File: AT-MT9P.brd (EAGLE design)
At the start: 38 x 34 mm, 3 parts

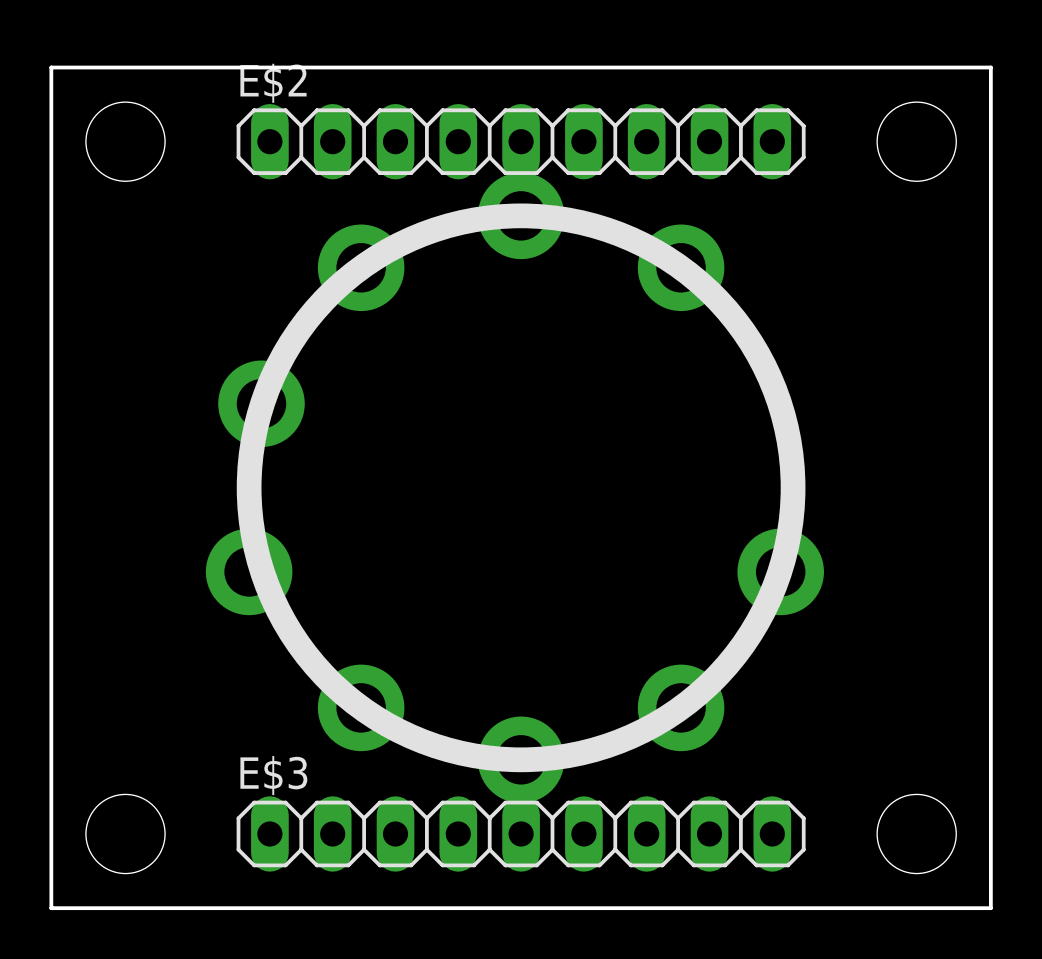
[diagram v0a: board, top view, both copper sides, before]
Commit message: [fix]ピンヘッダが逆だった
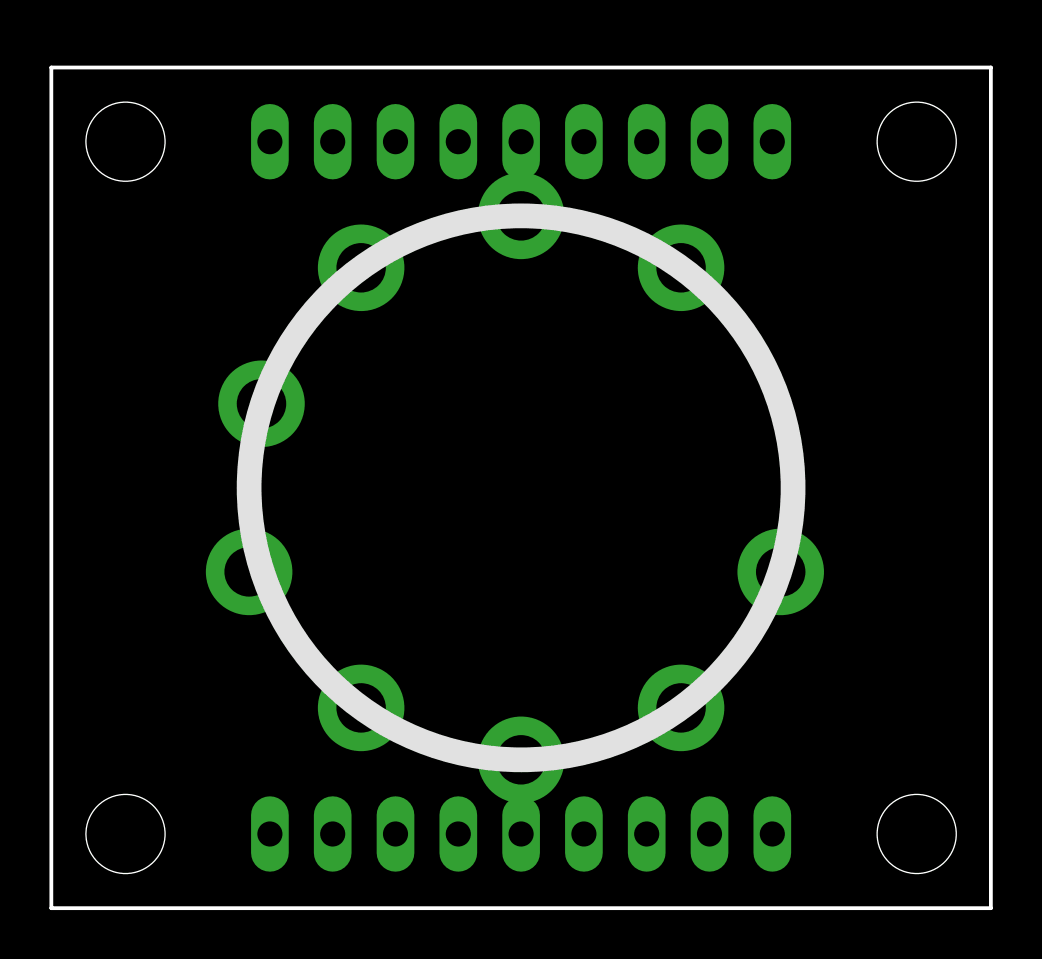
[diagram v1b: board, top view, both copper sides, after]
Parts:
- flipped E$2 to the bottom
- flipped E$3 to the bottom
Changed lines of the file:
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@@
 </layers>
 <board>
-<fusionsync huburn="a.cGVyc29uYWw6dWUyZDlmMDVj" projecturn="a.cGVyc29uYWw6dWUyZDlmMDVjIzIwMTgxMjMwMTY3NjU5OTU2" f3durn="urn:adsk.wipprod:dm.lineage:NYwnF4SlTam06u2sAxt6oQ" pcbguid="4a25c511-59d3-438b-b27a-b959e0cbe7cb" lastpulledtime="" lastsyncedchangeguid="c63ba295-d3e6-aa65-7cf6-419a23981807"/>
+<fusionsync huburn="a.cGVyc29uYWw6dWUyZDlmMDVj" projecturn="a.cGVyc29uYWw6dWUyZDlmMDVjIzIwMTgxMjMwMTY3NjU5OTU2" f3durn="urn:adsk.wipprod:dm.lineage:NYwnF4SlTam06u2sAxt6oQ" pcbguid="4a25c511-59d3-438b-b27a-b959e0cbe7cb" lastpulledtime="" lastsyncedchangeguid="31855698-3f46-38bd-1312-e686bdc45d92"/>
 <plain>
 <wire x1="-19" y1="17" x2="-19" y2="-17" width="0.1524" layer="20"/>
@@
 <elements>
 <element name="E$1" library="VacuumTube" library_urn="urn:adsk.eagle:library:8044196" package="NOVAL_SOCKET" package3d_urn="urn:adsk.eagle:package:8044357/4" value="" x="0" y="0" smashed="yes"/>
-<element name="E$2" library="pinhead" library_urn="urn:adsk.eagle:library:325" package="1X09" package3d_urn="urn:adsk.eagle:package:22483/2" value="" x="0" y="14" smashed="yes">
-<attribute name="NAME" x="-11.5062" y="15.8288" size="1.27" layer="25" ratio="10"/>
-<attribute name="VALUE" x="-11.43" y="10.825" size="1.27" layer="27"/>
+<element name="E$2" library="pinhead" library_urn="urn:adsk.eagle:library:325" package="1X09" package3d_urn="urn:adsk.eagle:package:22483/2" value="" x="0" y="14" smashed="yes" rot="MR0">
+<attribute name="NAME" x="11.5062" y="15.8288" size="1.27" layer="26" ratio="10" rot="MR0"/>
+<attribute name="VALUE" x="11.43" y="10.825" size="1.27" layer="28" rot="MR0"/>
 </element>
-<element name="E$3" library="pinhead" library_urn="urn:adsk.eagle:library:325" package="1X09" package3d_urn="urn:adsk.eagle:package:22483/2" value="" x="0" y="-14" smashed="yes">
-<attribute name="NAME" x="-11.5062" y="-12.1712" size="1.27" layer="25" ratio="10"/>
-<attribute name="VALUE" x="-11.43" y="-17.175" size="1.27" layer="27"/>
+<element name="E$3" library="pinhead" library_urn="urn:adsk.eagle:library:325" package="1X09" package3d_urn="urn:adsk.eagle:package:22483/2" value="" x="0" y="-14" smashed="yes" rot="MR0">
+<attribute name="NAME" x="11.5062" y="-12.1712" size="1.27" layer="26" ratio="10" rot="MR0"/>
+<attribute name="VALUE" x="11.43" y="-17.175" size="1.27" layer="28" rot="MR0"/>
 </element>
 </elements>
